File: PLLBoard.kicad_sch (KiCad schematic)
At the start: 28 parts, among them J1 Conn_01x07, J2 Conn_Coaxial, J3 Conn_Coaxial, J4 Conn_Coaxial, Q1 2N7002, Q2 2N7002, U1 AMS1117-3.3, U2 Si5351A-B-GT, Y1 25 MHz, Y2 25 MHz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

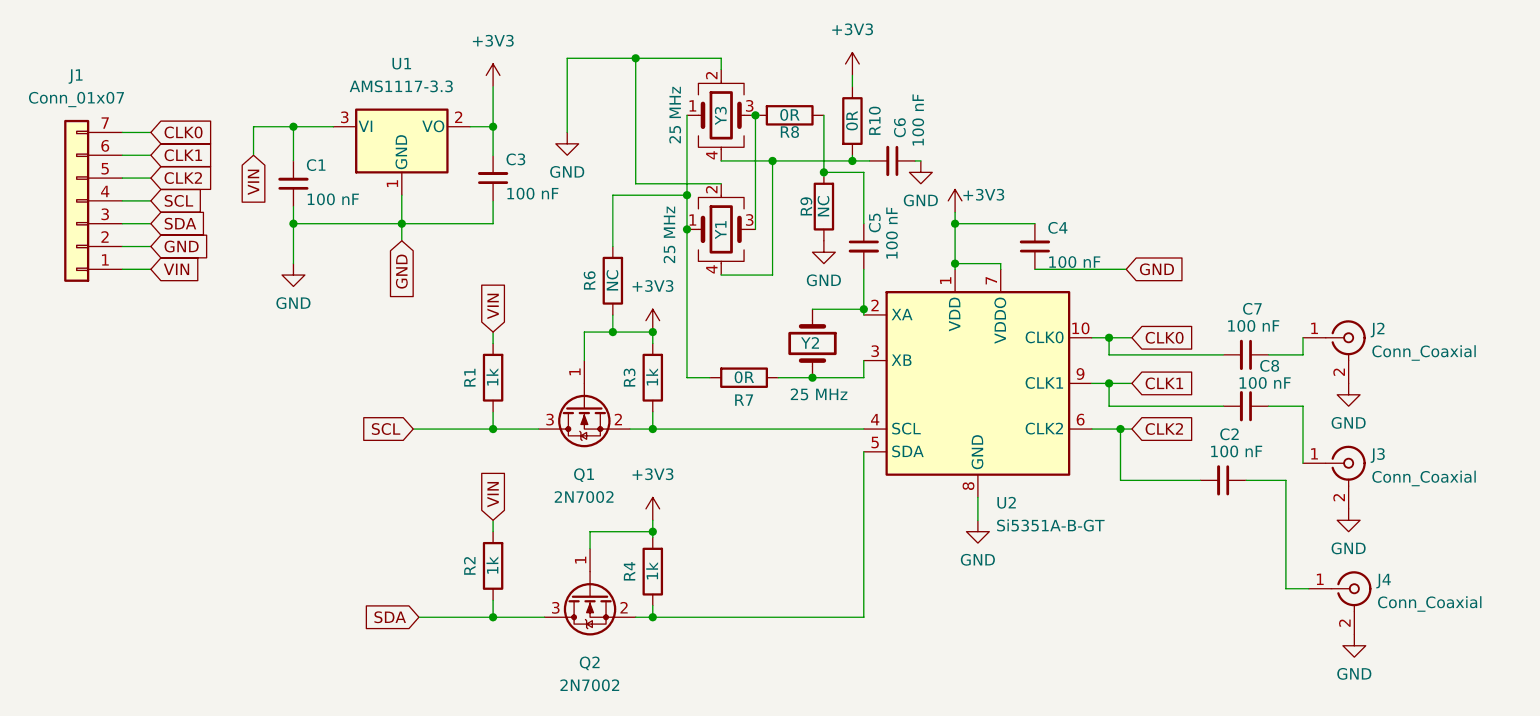
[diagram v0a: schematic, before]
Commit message: Shrink PLL board, remove resistor
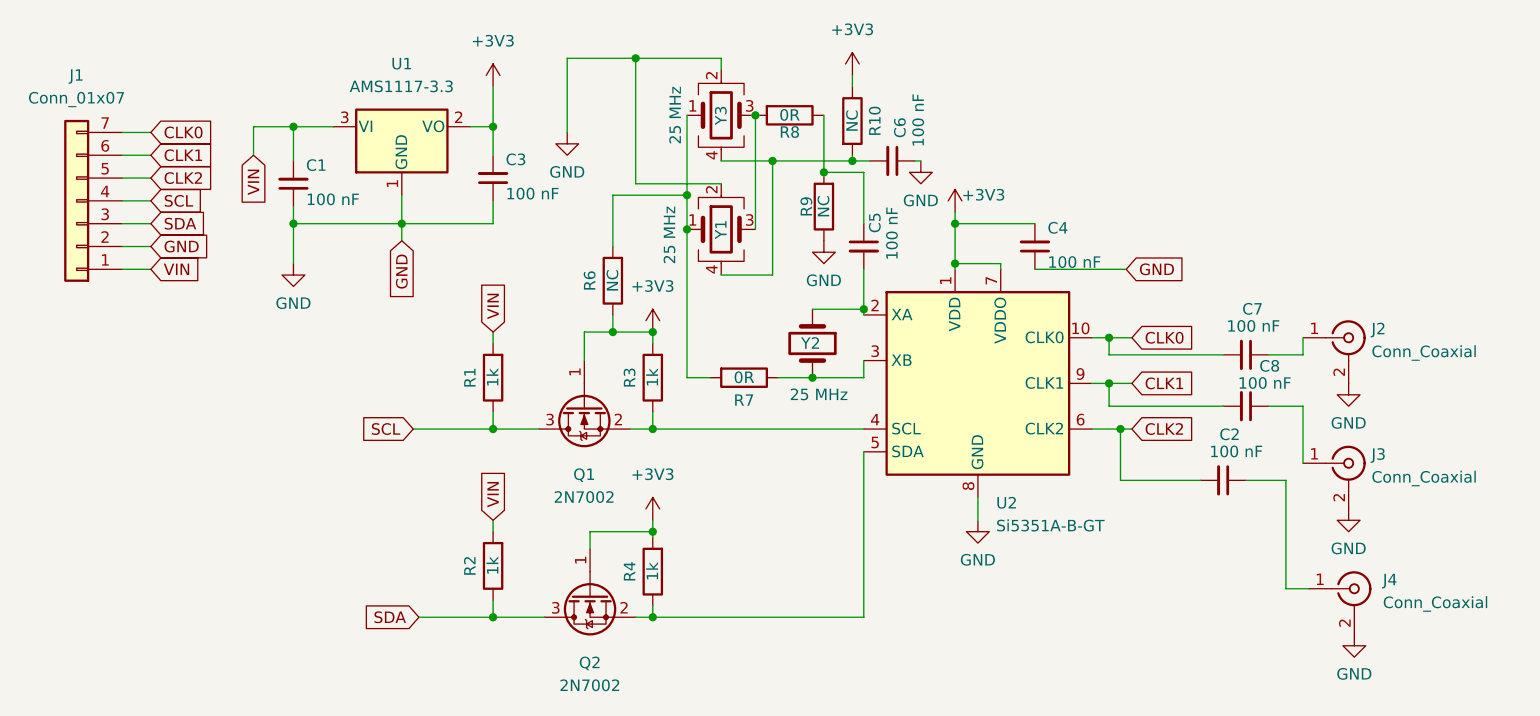
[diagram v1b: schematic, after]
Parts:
- J2, J3, J4: footprint Connector_Coaxial:SMA_Amphenol_132289_EdgeMount -> PLLBoard:SMA_Amphenol_132289_EdgeMount_Wide
- R10: value 0R -> NC; LCSC C17477 -> (none)
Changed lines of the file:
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@@
       (effects (font (size 1.27 1.27)) (justify left))
     )
-    (property "Footprint" "Connector_Coaxial:SMA_Amphenol_132289_EdgeMount" (id 2) (at 166.37 55.88 0)
+    (property "Footprint" "PLLBoard:SMA_Amphenol_132289_EdgeMount_Wide" (id 2) (at 166.37 55.88 0)
       (effects (font (size 1.27 1.27)) hide)
     )
@@
     (in_bom yes) (on_board yes)
     (property "Reference" "R10" (id 0) (at 113.665 31.75 90))
-    (property "Value" "0R" (id 1) (at 111.125 31.75 90))
+    (property "Value" "NC" (id 1) (at 111.125 31.75 90))
     (property "Footprint" "Resistor_SMD:R_0805_2012Metric_Pad1.20x1.40mm_HandSolder" (id 2) (at 109.347 31.75 90)
       (effects (font (size 1.27 1.27)) hide)
@@
       (effects (font (size 1.27 1.27)) hide)
     )
-    (property "LCSC" "C17477 " (id 4) (at 111.125 31.75 90)
+    (property "LCSC" "" (id 4) (at 111.125 31.75 90)
       (effects (font (size 1.27 1.27)) hide)
     )
@@
   (symbol (lib_id "Connector:Conn_Coaxial") (at 167.005 83.82 0) (unit 1)
     (in_bom yes) (on_board yes) (fields_autoplaced)
-    (property "Reference" "J4" (id 0) (at 169.545 82.8431 0)
-      (effects (font (size 1.27 1.27)) (justify left))
-    )
-    (property "Value" "Conn_Coaxial" (id 1) (at 169.545 85.3831 0)
-      (effects (font (size 1.27 1.27)) (justify left))
-    )
-    (property "Footprint" "Connector_Coaxial:SMA_Amphenol_132289_EdgeMount" (id 2) (at 167.005 83.82 0)
+    (property "Reference" "J4" (id 0) (at 170.18 82.8431 0)
+      (effects (font (size 1.27 1.27)) (justify left))
+    )
+    (property "Value" "Conn_Coaxial" (id 1) (at 170.18 85.3831 0)
+      (effects (font (size 1.27 1.27)) (justify left))
+    )
+    (property "Footprint" "PLLBoard:SMA_Amphenol_132289_EdgeMount_Wide" (id 2) (at 167.005 83.82 0)
       (effects (font (size 1.27 1.27)) hide)
     )
@@
       (effects (font (size 1.27 1.27)) (justify left))
     )
-    (property "Footprint" "Connector_Coaxial:SMA_Amphenol_132289_EdgeMount" (id 2) (at 166.37 69.85 0)
+    (property "Footprint" "PLLBoard:SMA_Amphenol_132289_EdgeMount_Wide" (id 2) (at 166.37 69.85 0)
       (effects (font (size 1.27 1.27)) hide)
     )
@@
     )
     (path "/35508218-fea8-4206-b85b-deef0d09abbe"
-      (reference "J2") (unit 1) (value "Conn_Coaxial") (footprint "Connector_Coaxial:SMA_Amphenol_132289_EdgeMount")
+      (reference "J2") (unit 1) (value "Conn_Coaxial") (footprint "PLLBoard:SMA_Amphenol_132289_EdgeMount_Wide")
     )
     (path "/8c414c3a-7354-4d9d-90cc-698861d84511"
-      (reference "J3") (unit 1) (value "Conn_Coaxial") (footprint "Connector_Coaxial:SMA_Amphenol_132289_EdgeMount")
+      (reference "J3") (unit 1) (value "Conn_Coaxial") (footprint "PLLBoard:SMA_Amphenol_132289_EdgeMount_Wide")
     )
     (path "/7dc062c0-45ef-4bf4-9d1b-b428f18b3b1e"
-      (reference "J4") (unit 1) (value "Conn_Coaxial") (footprint "Connector_Coaxial:SMA_Amphenol_132289_EdgeMount")
+      (reference "J4") (unit 1) (value "Conn_Coaxial") (footprint "PLLBoard:SMA_Amphenol_132289_EdgeMount_Wide")
     )
     (path "/4ef71e27-59c3-48ef-87f6-1896b1985788"
@@
     )
     (path "/3c4cb38b-1e67-4386-8485-cab1afc59257"
-      (reference "R10") (unit 1) (value "0R") (footprint "Resistor_SMD:R_0805_2012Metric_Pad1.20x1.40mm_HandSolder")
+      (reference "R10") (unit 1) (value "NC") (footprint "Resistor_SMD:R_0805_2012Metric_Pad1.20x1.40mm_HandSolder")
     )
     (path "/d48499d8-36a9-4cd7-a4e4-067aa1d47308"
